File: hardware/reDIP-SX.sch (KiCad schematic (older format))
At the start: 82 parts, among them J1 DX07S016JA1, J10 Conn_01x01, J11 Conn_01x01, J2 Conn_01x01, J3 Conn_01x01, J4 Conn_01x01, J5 Conn_01x06, J6 Conn_01x06, J7 Conn_01x10, J8 Conn_01x10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

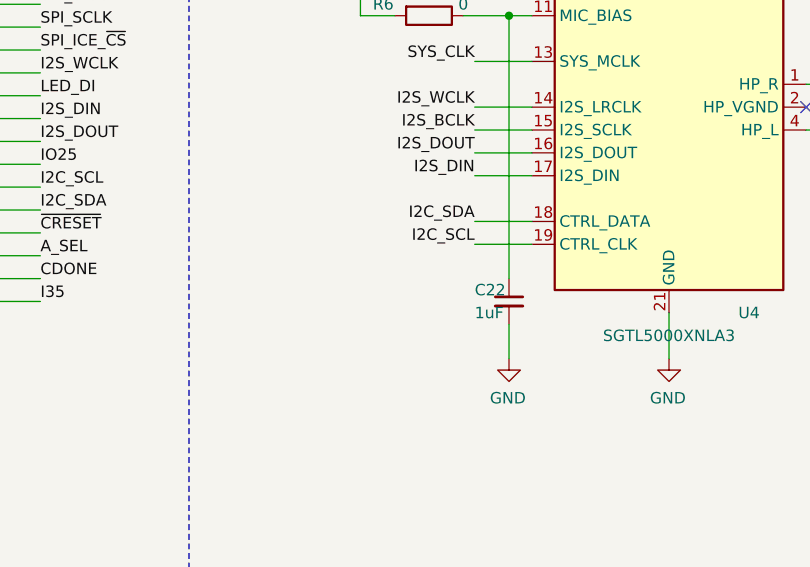
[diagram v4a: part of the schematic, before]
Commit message: Reduced layer count from 6 to 4
As originally suggested by @smunaut for reDIP SID.
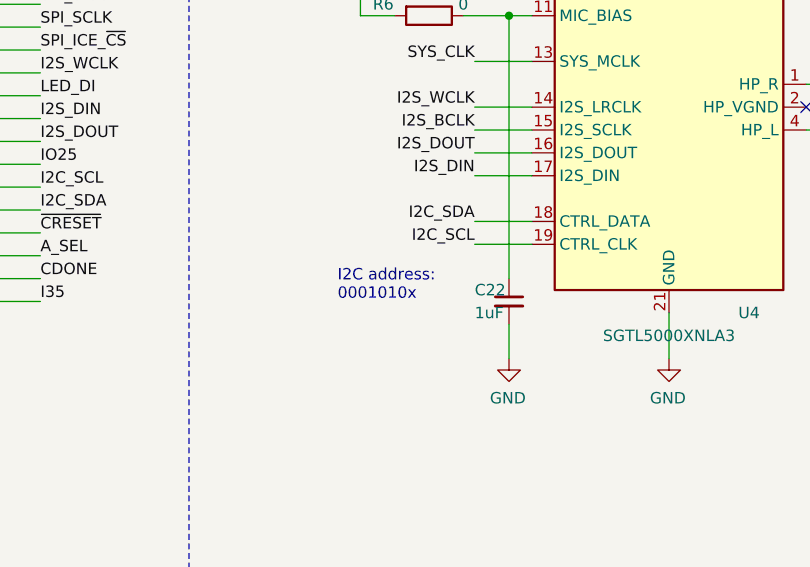
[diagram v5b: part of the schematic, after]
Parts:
- U4: Notes ALTERNATIVE PART #: SGTL5000XNLA3R2 -> ALTERNATIVE PART #: SGTL5000XNLA3; PN SGTL5000XNLA3 -> SGTL5000XNLA3R2
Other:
- note added: "I2C address:\n0001010x"
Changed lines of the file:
@@
 Sheet 1 1
 Title "reDIP SX"
-Date "2021-05-01"
-Rev "0.2"
+Date "2021-05-13"
+Rev "0.3"
 Comp "Nimrod"
 Comment1 "© 2020 - 2021 Dag Lem"
@@
 F 4 "IC AUDIO CODEC UQFN-20" H 13900 3700 50  0001 C CNN "Description"
 F 5 "NXP" H 13900 3700 50  0001 C CNN "Mfg"
-F 6 "SGTL5000XNLA3" H 13900 3700 50  0001 C CNN "PN"
-F 7 "ALTERNATIVE PART #: SGTL5000XNLA3R2" H 13900 3700 50  0001 C CNN "Notes"
+F 6 "SGTL5000XNLA3R2" H 13900 3700 50  0001 C CNN "PN"
+F 7 "ALTERNATIVE PART #: SGTL5000XNLA3" H 13900 3700 50  0001 C CNN "Notes"
 	1    13900 3700
 	1    0    0    -1
@@
 Text Notes 6950 11050 0    50   ~ 0
 Note: If the PLL is used, G0 and G1\nbecome output-only.\nThe ESP32 APLL may alternatively be used\nto generate a custom clock frequency.\nIn this case, the I2S master clock must\nbe generated by the SGTL5000 PLL
+Text Notes 12450 4750 0    50   ~ 0
+I2C address:\n0001010x
 $EndSCHEMATC
